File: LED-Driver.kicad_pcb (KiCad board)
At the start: 2 copper layers, 58.2 x 53.2 mm, 9 parts, among them J1 Conn_01x04, J2 Barrel_Jack_Switch, Q1 NTE289, Q2 NTE289, Q3 NTE289, U1 Pico

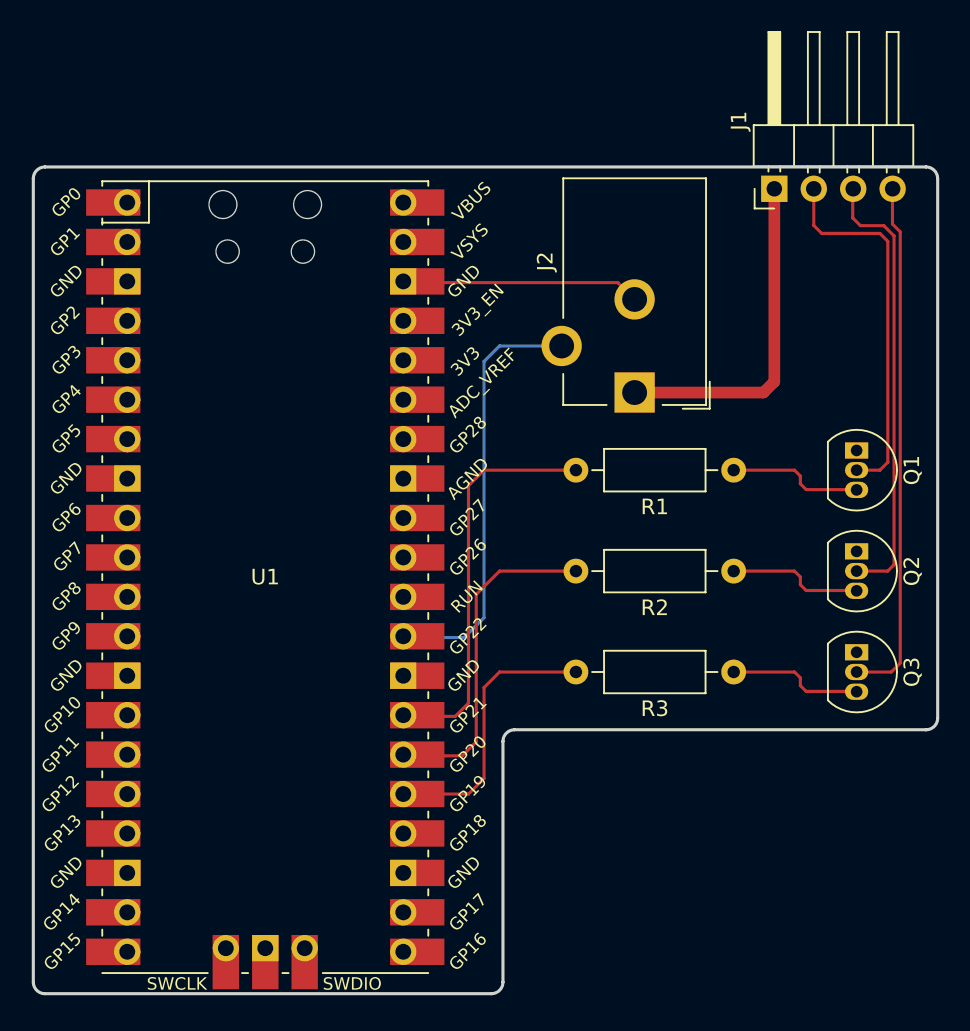
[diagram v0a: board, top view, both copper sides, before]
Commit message: Change edge clearance
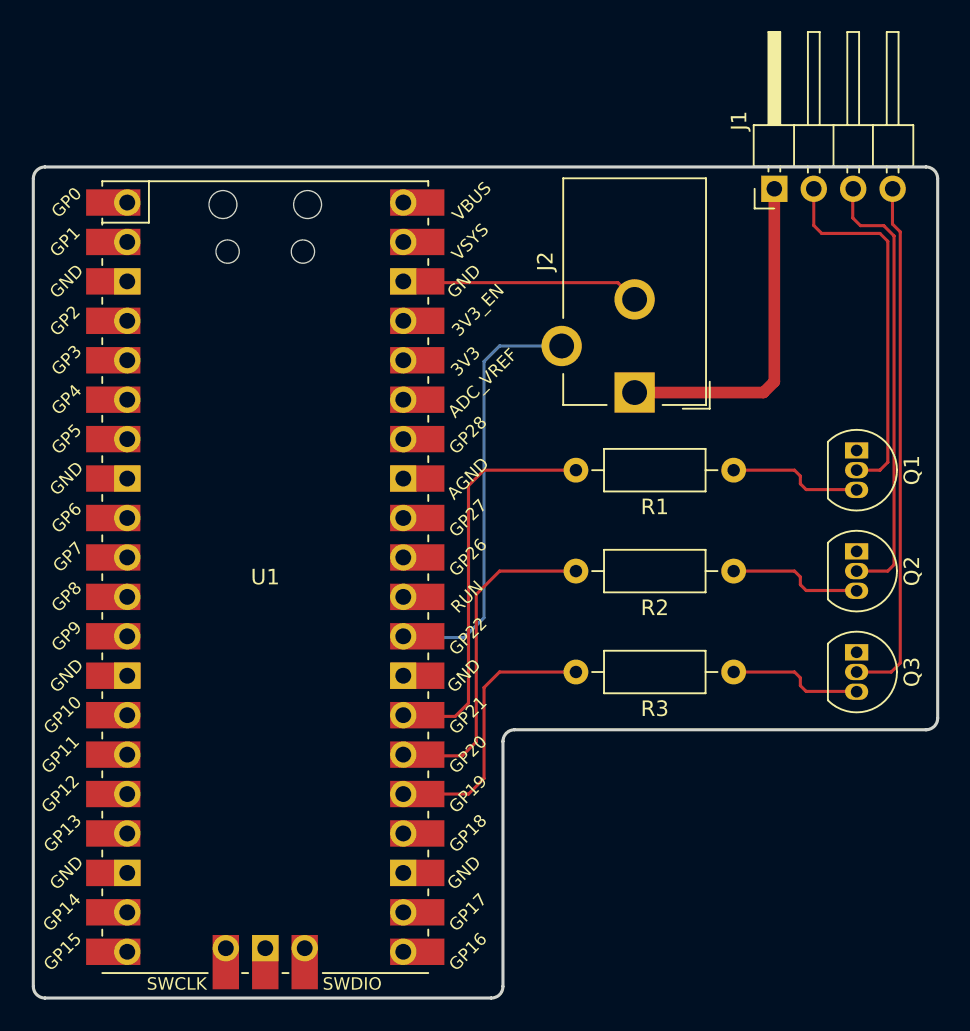
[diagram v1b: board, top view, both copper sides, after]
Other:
- board size 58.2 x 53.2 mm -> 58.2 x 53.5 mm
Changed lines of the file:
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@@
 	)
 	(gr_line
-		(start 13.30967 65.71967)
-		(end 42.05967 65.71967)
+		(start 13.30967 66)
+		(end 42.05967 66)
 		(stroke
 			(width 0.2)
@@
 	)
 	(gr_arc
-		(start 42.80967 64.96967)
-		(mid 42.59 65.5)
-		(end 42.05967 65.71967)
+		(start 42.80967 65.25)
+		(mid 42.590009 65.780339)
+		(end 42.05967 66)
 		(stroke
 			(width 0.2)
@@
 	(gr_line
 		(start 42.80967 49.46967)
-		(end 42.80967 64.96967)
+		(end 42.80967 65.25)
 		(stroke
 			(width 0.2)
@@
 	)
 	(gr_arc
-		(start 13.30967 65.71967)
-		(mid 12.77934 65.5)
-		(end 12.55967 64.96967)
+		(start 13.30967 66)
+		(mid 12.77937 65.780318)
+		(end 12.55967 65.25)
 		(stroke
 			(width 0.2)
@@
 	(gr_line
 		(start 12.55967 13.21967)
-		(end 12.55967 64.96967)
+		(end 12.55967 65.25)
 		(stroke
 			(width 0.2)
